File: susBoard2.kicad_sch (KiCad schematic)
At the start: 0 parts

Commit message: PCIe and placed microcontroller
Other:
- added sheet PCIE (PCIE.kicad_sch)
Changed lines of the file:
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@@
 	(generator_version "9.0")
 	(paper "A4")
+	(sheet
+		(at 233.68 22.86)
+		(size 38.1 44.45)
+		(exclude_from_sim no)
+		(in_bom yes)
+		(on_board yes)
+		(dnp no)
+		(fields_autoplaced yes)
+		(stroke
+			(width 0.1524)
+			(type solid)
+		)
+		(fill
+			(color 0 0 0 0.0000)
+		)
+		(property "Sheetname" "PCIE"
+			(at 233.68 22.1484 0)
+			(effects
+				(font
+					(size 1.27 1.27)
+				)
+				(justify left bottom)
+			)
+		)
+		(property "Sheetfile" "PCIE.kicad_sch"
+			(at 233.68 67.8946 0)
+			(effects
+				(font
+					(size 1.27 1.27)
+				)
+				(justify left top)
+			)
+		)
+		(instances
+			(project "susBoard2"
+				(path "/dea87457-738f-4c5a-8d68-6b57d3b491ea"
+					(page "2")
+				)
+			)
+		)
+	)
 	(sheet_instances
 		(path "/"

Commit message: started adding things to the STM32
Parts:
- added C1: C_0.1uF_16V, OEM:C_0603_1608Metric, symbol OEM:C_0.1uF_16V_0603
- added C2, C3, C7: C_0.1uF, OEM:C_0603_1608Metric, symbol OEM:C_0.1uF_16V_0603
- added C4: C_4.7uF, OEM:C_0603_1608Metric, symbol OEM:C_4.7uF_25V_0603
- added C5: C_1uF, OEM:C_0603_1608Metric, symbol OEM:C_1uF_25V_0603
- added C6: C_10nF, OEM:C_0603_1608Metric, symbol OEM:C_10nF_50V_0603
- added J2: J_Programming_Pin_Header, stm32g441kbt6:Programming_Pin_Header_Keyed, symbol OEM:J_Programming_Pin_Header
- added U1: MCP2561-E_SN, OEM:SOIC-8_3.9x4.9mm_P1.27mm, symbol OEM:U_CAN-Transceiver_MCP2561-E_SN_SOIC-8
- added U2: STM32G441KBT6, OEM:LQFP-32_7x7mm_P0.8mm, symbol OEM:U_MCU_STM32G441KBT6_32-LQFP
- added Y1: X_16MHz_18pF, OEM:FA238160000MBC0 (X_16MHz_18pF_SMD - FA-238_16.0000MB-C0), symbol OEM:X_16MHz_18pF_SMD
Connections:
- new net +3V3: C2.1, C3.1, C4.1, C5.1, C6.1, J2.3 (Pin_3), U2.1 (VDD), U2.15 (VDDA), U2.17 (VDD)
- new net +5V: C1.1, U1.3 (VDD)
- new net CAN+: U1.7 (CANH)
- new net CAN-: U1.6 (CANL)
- new net CAN_RX: U1.4 (RXD), U2.21 ((FDCAN1_RX/GPIO_EXTI11)PA11)
- new net CAN_TX: U1.1 (TXD), U2.22 ((FDCAN1_TX/GPIO_EXTI12)PA12)
- new net GND: C1.2, C2.2, C3.2, C4.2, C5.2, C6.2, C7.2, J2.2 (Pin_2), U1.2 (VSS), U1.8 (STBY), U2.14 (VSSA), U2.16 (VSS), U2.32 (VSS)
- new net NRST: C7.1, J2.4 (Pin_4), U2.4 ((GPIO_EXTI10)PG10-NRST)
- new net SWCLK: J2.5 (Pin_5), U2.24 ((SYS_JTCK-SWCLK/GPIO_EXTI14)PA14)
- new net SWDIO: J2.1 (Pin_1), U2.23 ((SYS_JTMS-SWDIO/GPIO_EXTI13)PA13)
- no-connect marks 0 -> 1
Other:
- sheet PCIE ports: added 3V3, 5V, CAN+, CAN-, GND, INPUT_1, INPUT_2, INPUT_3, INPUT_4, INPUT_5; removed none

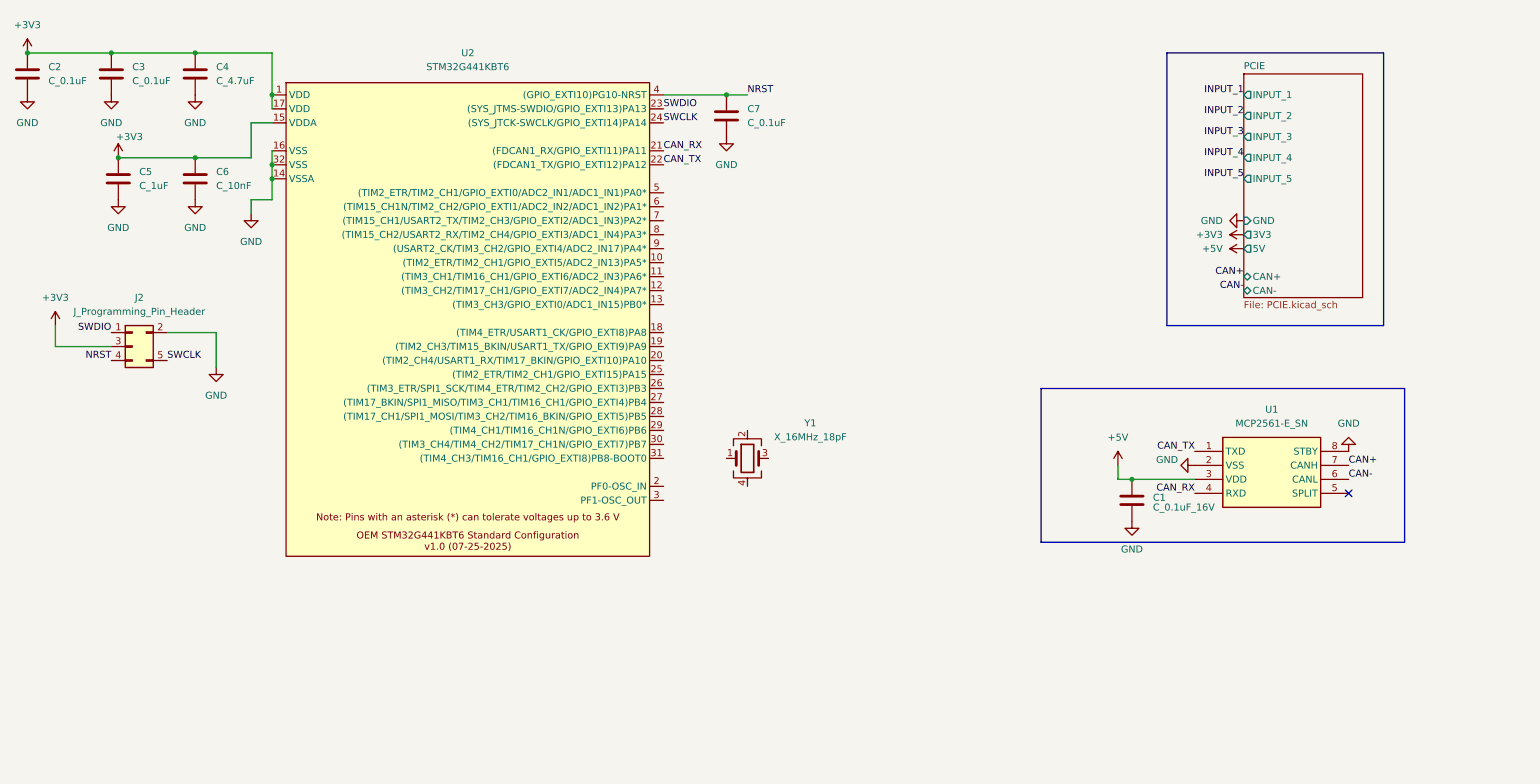
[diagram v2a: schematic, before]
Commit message: finished STM32 boiler plate
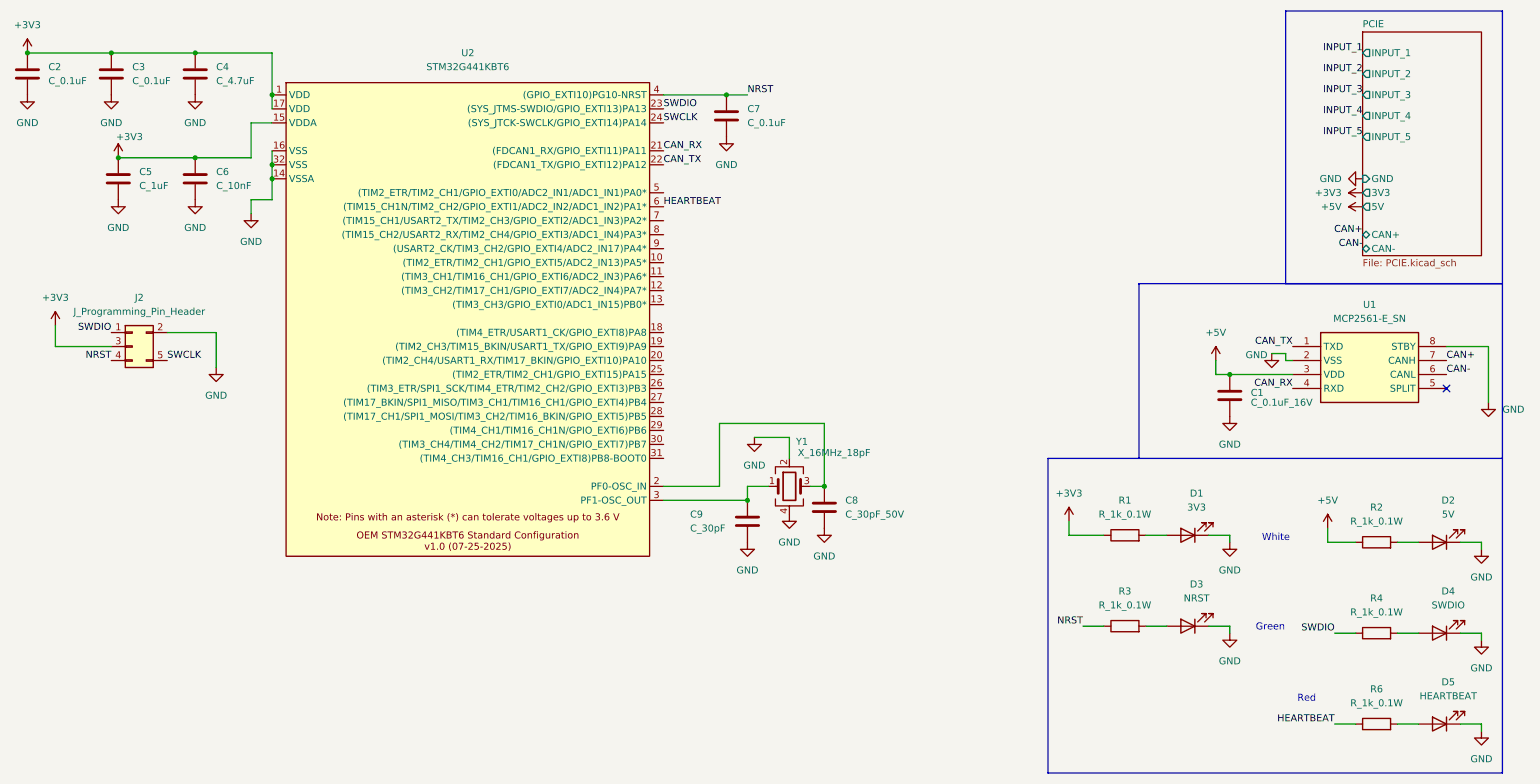
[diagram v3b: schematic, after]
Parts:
- added C8: C_30pF_50V, OEM:C_0603_1608Metric, symbol OEM:C_30pF_50V_0603
- added C9: C_30pF, OEM:C_0603_1608Metric, symbol OEM:C_30pF_50V_0603
- added D1: 3V3, OEM:D_0805_2012Metric, symbol OEM:D_LED_White_0805
- added D2: 5V, OEM:D_0805_2012Metric, symbol OEM:D_LED_White_0805
- added D3: NRST, OEM:D_0805_2012Metric, symbol OEM:D_LED_Green_0805
- added D4: SWDIO, OEM:D_0805_2012Metric, symbol OEM:D_LED_Green_0805
- added D5: HEARTBEAT, OEM:D_0805_2012Metric, symbol OEM:D_LED_Red_0805
- added R1, R2, R3, R4, R6: R_1k_0.1W, OEM:R_0603_1608Metric, symbol OEM:R_1k_0.1W_0603
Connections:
- net +3V3: now also R1.1
- net +5V: now also R2.1
- net GND: now also Y1.2, Y1.4, C8.2, C9.1, D1.1 (K), D2.1 (K), D3.1 (K), D4.1 (K), D5.1 (K)
- net NRST: now also R3.1
- net SWDIO: now also R4.1
- net at Y1.1: now also U2.3 (PF1-OSC_OUT), C9.2
- net at Y1.3: now also U2.2 (PF0-OSC_IN), C8.1
- net HEARTBEAT: now reaches U2.6 ((TIM15_CH1N/TIM2_CH2/GPIO_EXTI1/ADC2_IN2/ADC1_IN2)PA1*)
- net HEARTBEAT: now also R6.1
- new net: D5.2 (A), R6.2
- new net: D1.2 (A), R1.2
- new net: D2.2 (A), R2.2
- new net: D3.2 (A), R3.2
- new net: D4.2 (A), R4.2
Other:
- note added: "Green"
- note added: "Red"
- note added: "White"
- moved on the sheet: C1, U1, Y1
